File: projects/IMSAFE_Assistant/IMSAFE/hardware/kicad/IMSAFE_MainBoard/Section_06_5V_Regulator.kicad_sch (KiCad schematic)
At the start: 10 parts, among them U8 TPS62130RGTR

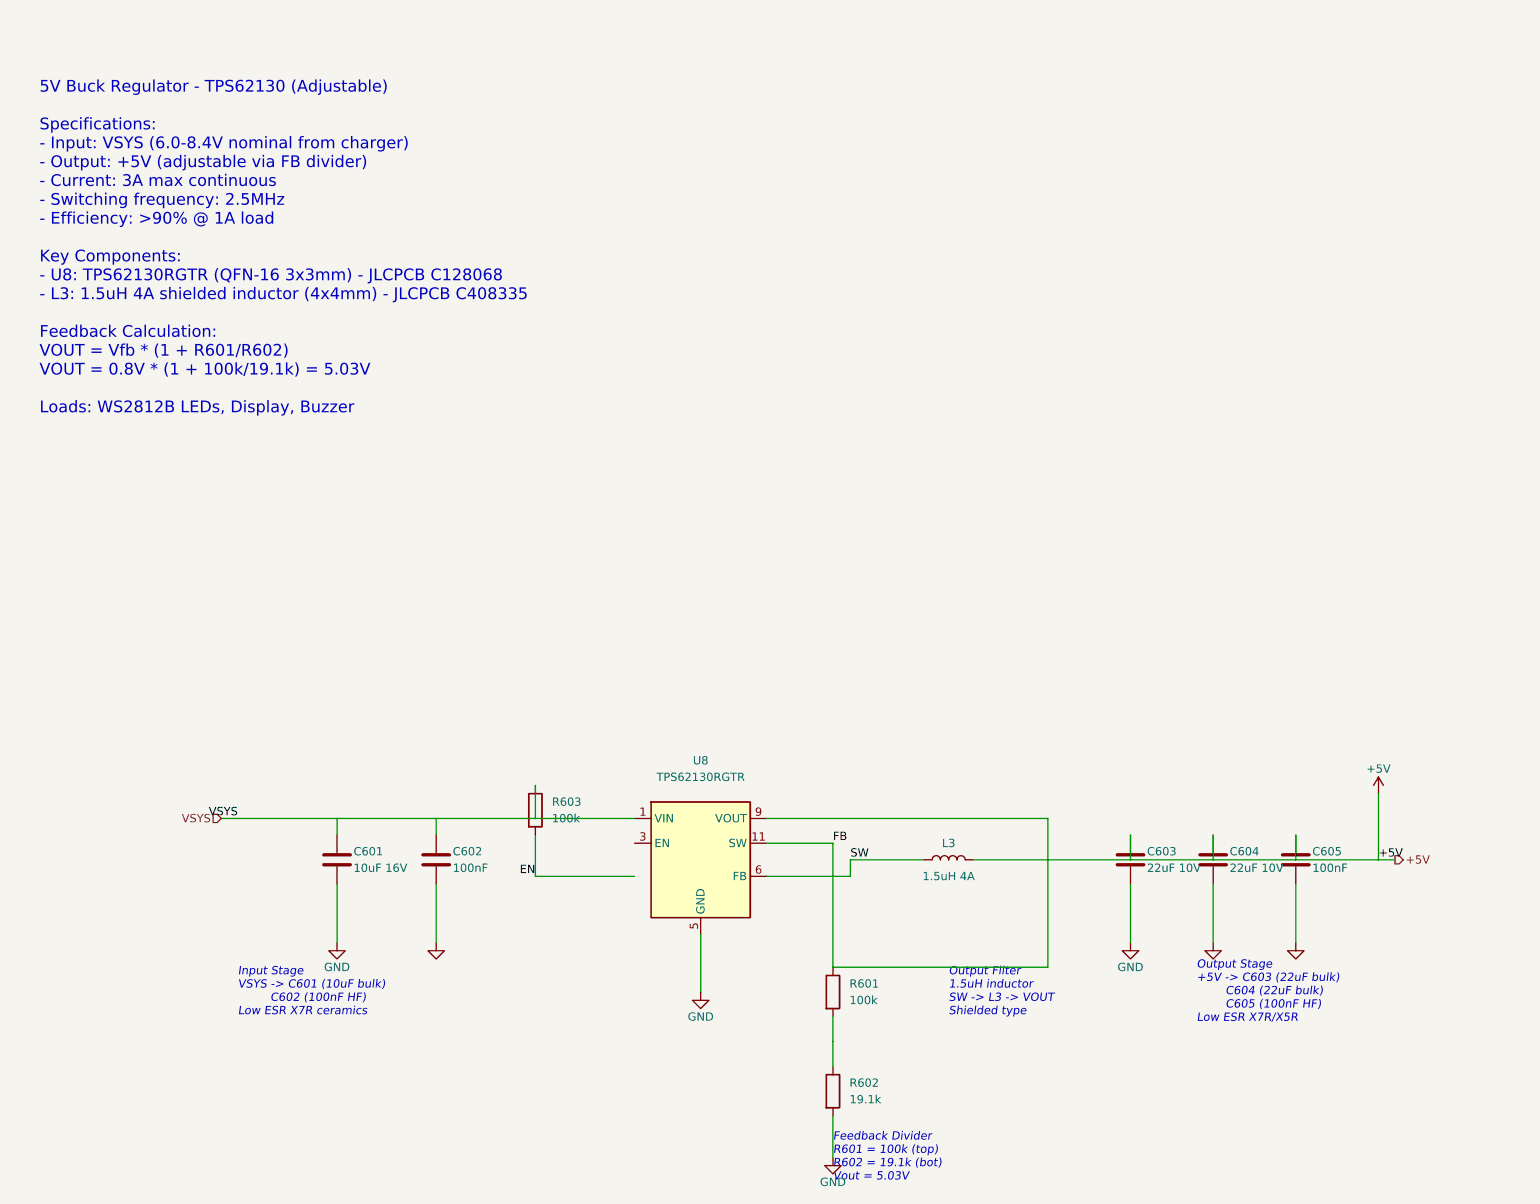
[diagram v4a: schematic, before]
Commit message: Update KiCad schematics and add analysis files
- Update all MainBoard schematic sections with component placement
- Add ERC reports and analysis scripts for schematic validation
- Update Radar Interface and SwitchLED Board projects
- Sync KiCad project files with latest session changes

Co-Authored-By: Claude Opus 4.5 <noreply@anthropic.com>
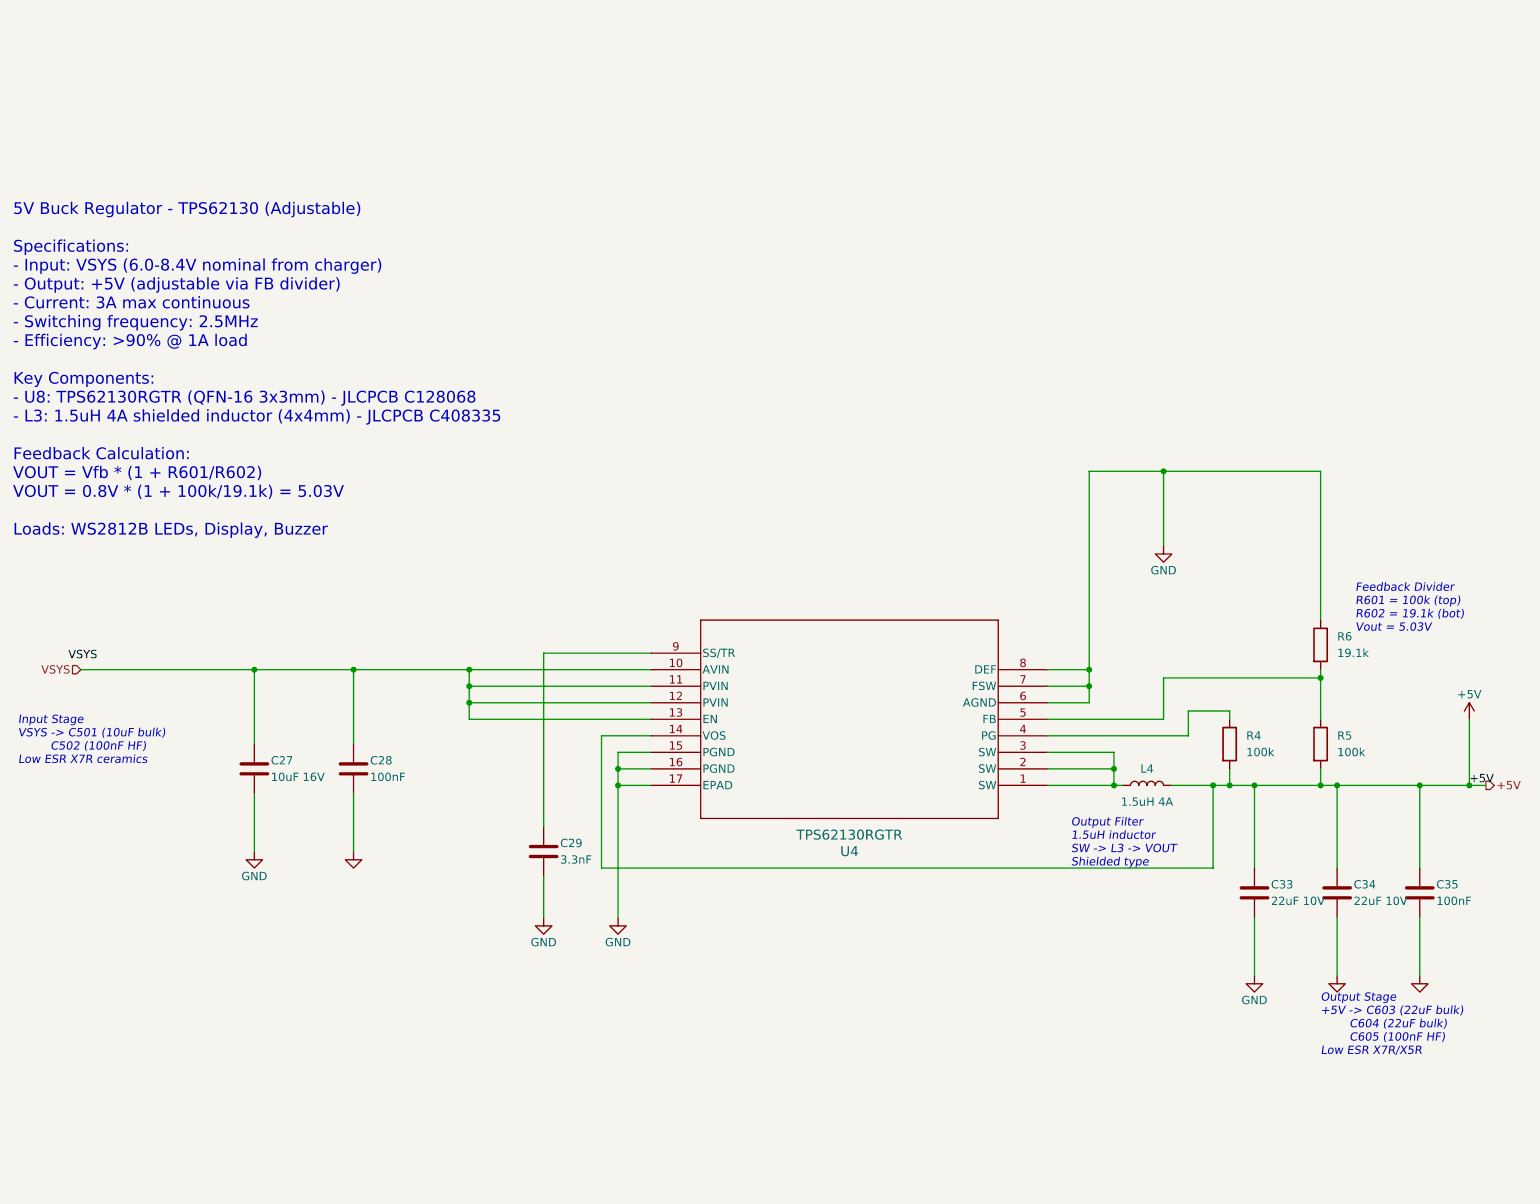
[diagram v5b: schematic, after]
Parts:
- removed C601: 10uF 16V, Capacitor_SMD:C_0805_2012Metric, symbol Device:C
- removed C602, C605: 100nF, Capacitor_SMD:C_0603_1608Metric, symbol Device:C
- removed C603, C604: 22uF 10V, Capacitor_SMD:C_0805_2012Metric, symbol Device:C
- removed L3: 1.5uH 4A, Inductor_SMD:L_4x4mm_H2.5mm, symbol Device:L
- removed R601, R603: 100k, Resistor_SMD:R_0603_1608Metric, symbol Device:R
- removed R602: 19.1k, Resistor_SMD:R_0603_1608Metric, symbol Device:R
- removed U8: TPS62130RGTR, Package_DFN_QFN:QFN-16-1EP_3x3mm_P0.5mm_EP1.8x1.8mm, symbol Regulator:TPS62130RGTR
- added C27: 10uF 16V, Capacitor_SMD:C_0805_2012Metric, symbol Device:C
- added C28, C35: 100nF, Capacitor_SMD:C_0603_1608Metric, symbol Device:C
- added C29: 3.3nF, Capacitor_SMD:C_0603_1608Metric, symbol Device:C
- added C33, C34: 22uF 10V, Capacitor_SMD:C_0805_2012Metric, symbol Device:C
- added L4: 1.5uH 4A, Inductor_SMD:L_4x4mm_H2.5mm, symbol Device:L
- added R4, R5: 100k, Resistor_SMD:R_0603_1608Metric, symbol Device:R
- added R6: 19.1k, Resistor_SMD:R_0603_1608Metric, symbol Device:R
- added U4: TPS62130RGTR, RGT16_1P7X1P7, symbol 1_New_library:TPS62130RGTR
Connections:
- net +5V: now also C33.1, C34.1, C35.1, L4.2, R4.2, R5.2, U4.14 (VOS)
- net GND: now also C27.2, C28.2, C29.2, C33.2, C34.2, C35.2, R6.1, U4.15 (PGND), U4.16 (PGND), U4.17 (EPAD), U4.6 (AGND), U4.7 (FSW), U4.8 (DEF)
- net VSYS: now also C27.1, C28.1, U4.10 (AVIN), U4.11 (PVIN), U4.12 (PVIN), U4.13 (EN)
- new net: R5.1, R6.2, U4.5 (FB)
- new net: C29.1, U4.9 (SS/TR)
- new net: L4.1, U4.1 (SW), U4.2 (SW), U4.3 (SW)
- new net: R4.1, U4.4 (PG)
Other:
- note added: "Input Stage VSYS -> C501 (10uF bulk) C502 (100nF HF) Low ESR X7R ceramics"
- note removed: "Input Stage VSYS -> C601 (10uF bulk) C602 (100nF HF) Low ESR X7R ceramics"
